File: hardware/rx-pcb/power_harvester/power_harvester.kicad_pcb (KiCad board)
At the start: 2 copper layers, 59 x 46.8 mm, 46 parts, among them J1 Conn_Coaxial_Small, J2 Conn_01x02_Pin, J3 Conn_Coaxial_Small, J4 Conn_Coaxial_Small

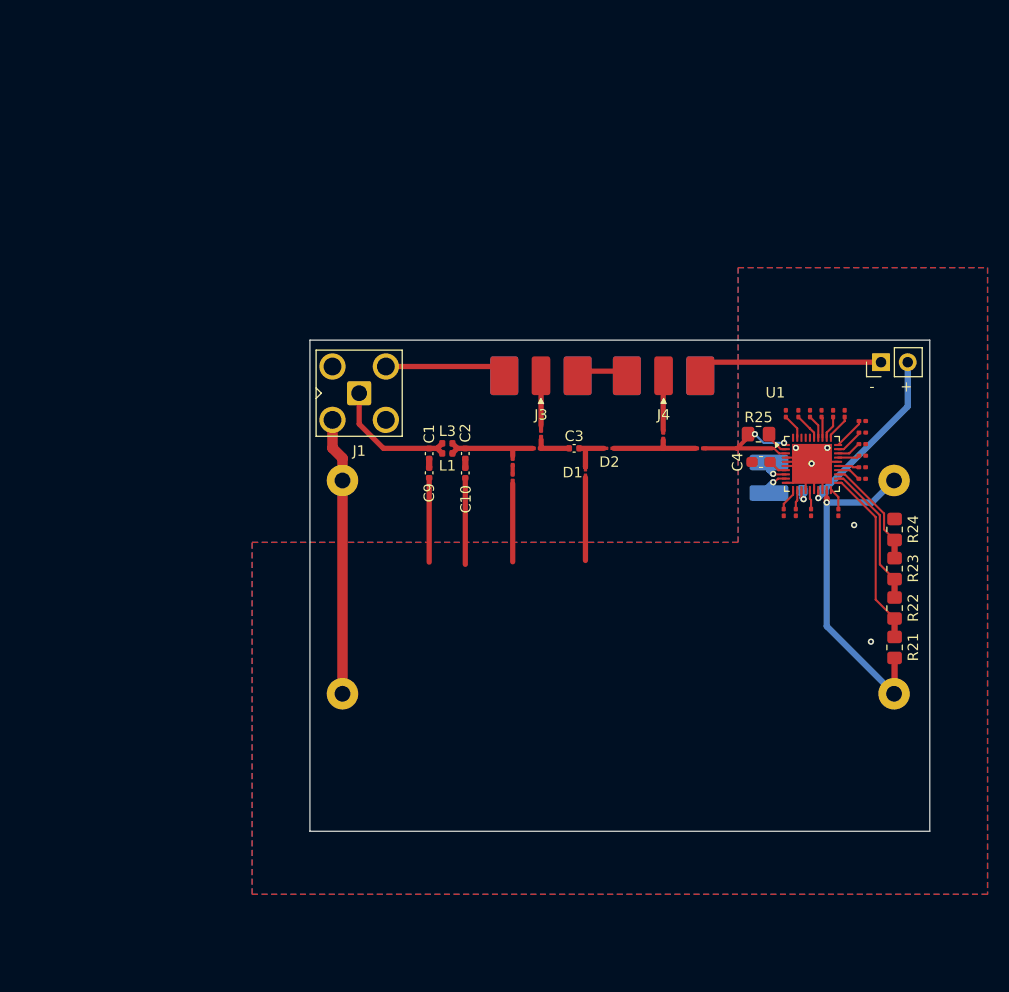
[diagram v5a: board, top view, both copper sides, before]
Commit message: updated PCB for weeks purchase
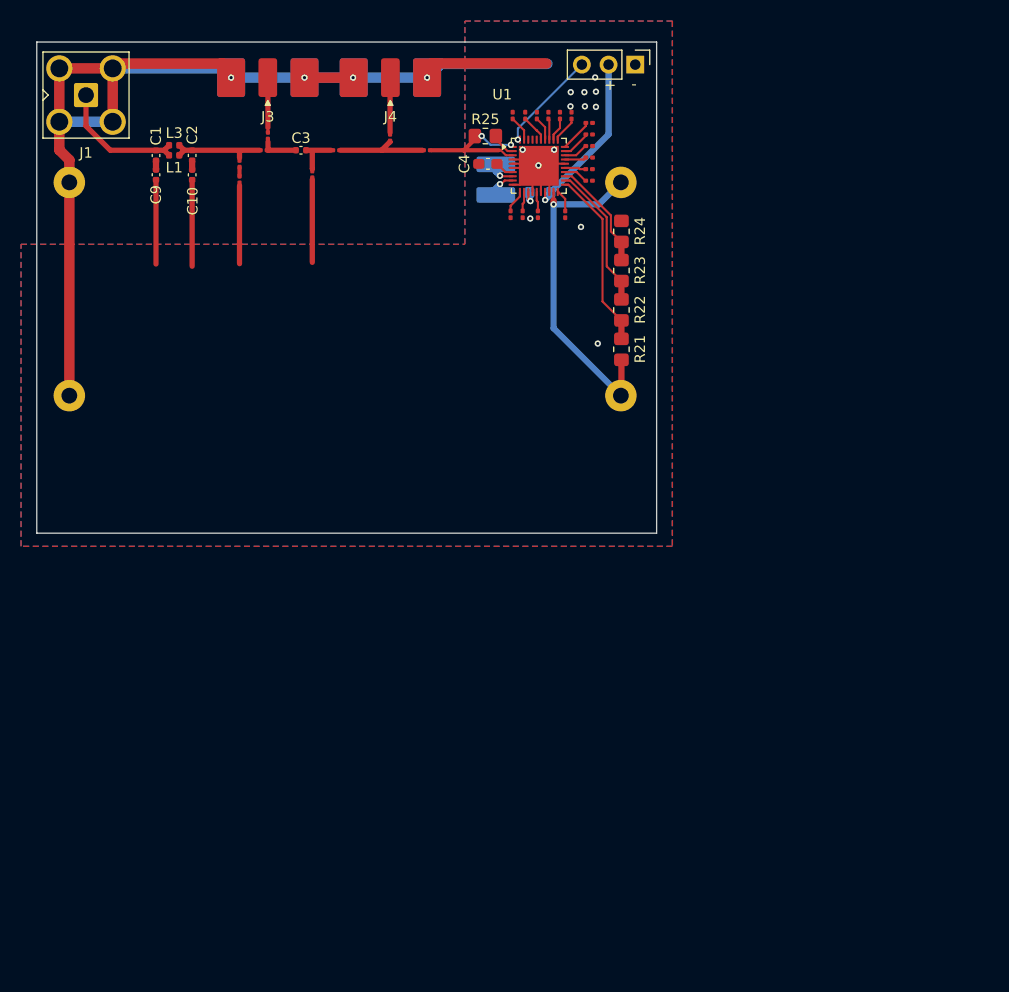
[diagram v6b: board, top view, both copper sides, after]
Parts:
- removed J2: Conn_01x02_Pin, Connector_PinHeader_2.54mm:PinHeader_1x02_P2.54mm_Vertical
- added J5: Conn_01x03_Pin, Connector_PinHeader_2.54mm:PinHeader_1x03_P2.54mm_Vertical, F.Cu at (127.5, 48.8)
- D1, D2: footprint power_harvester:JDH2S02SL -> power_harvester:R_0201_0603Metric_correctedclearance
- D3, D4: footprint Capacitor_SMD:C_0201_0603Metric -> power_harvester:R_0201_0603Metric_correctedclearance
- R1, R10, R11, R12, R13, R14, R15, R16, R2, R3, R4, R5, R6, R7, R8, R9: footprint Resistor_SMD:R_0201_0603Metric -> power_harvester:R_0201_0603Metric_correctedclearance
- R17, R18, R19, R20: footprint Resistor_SMD:R_0201_0603Metric_Pad0.64x0.40mm_HandSolder -> power_harvester:R_0201_0603Metric_correctedclearance
- moved C5 38.5 mm to (117.4, 60.1)
- moved C6 38.5 mm to (119.4, 60.1)
- moved R1 38.5 mm to (123.1, 56.5)
- moved R11 38.5 mm to (120.8, 63.0)
- moved C2 38.5 mm to (85.3, 57.4)
- moved R15 38.5 mm to (123.1, 54.3)
- moved R19 38.5 mm to (92.5, 55.5)
- moved R3 38.5 mm to (123.1, 57.6)
- moved R5 38.5 mm to (120.3, 53.6)
- moved R6 38.5 mm to (116.8, 63.0)
- moved R7 38.5 mm to (115.6, 63.0)
- moved R8 38.5 mm to (115.8, 53.6)
- moved R9 38.5 mm to (123.1, 55.4)
- moved C1 38.5 mm to (81.8, 57.4)
- moved C10 38.5 mm to (85.3, 59.3)
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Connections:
- U1 pad 40: unconnected-(U1-ST_STO-Pad40) -> /Pg
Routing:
- net GND: track 114.5 -> 173.3 mm, vias 5 -> 17
- net /Pg: track 0.00 -> 10.3 mm, vias 0 -> 1
- net /Po: track 17.4 -> 16.3 mm

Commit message: minor harvester updates
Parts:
- R12, R13, R4: value on -> off
- R14: value off -> on
- R21: value x -> 0
- R22: value x -> 19.5M
- R23: value x -> 100k
- R24: value x -> 5.6M
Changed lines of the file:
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@@
 		)
 		(property "Value" "off"
-			(at 0 1.05 180)
+			(at -1.705 0.025 180)
 			(layer "F.Fab")
 			(effects
@@
 			)
 		)
-		(property "Value" "x"
+		(property "Value" "100k"
 			(at 0 1.65 90)
 			(layer "F.Fab")
@@
 			)
 		)
-		(property "Value" "on"
-			(at 0 1.05 180)
+		(property "Value" "off"
+			(at -1.705 0.025 180)
 			(layer "F.Fab")
 			(effects
@@
 		)
 		(property "Value" "off"
-			(at 0 1.05 180)
+			(at -1.705 0.025 180)
 			(layer "F.Fab")
 			(effects
@@
 		)
 		(property "Value" "Conn_01x03_Pin"
-			(at 0 7.460001 90)
+			(at 4.55 0.465 90)
 			(layer "F.Fab")
+			(hide yes)
 			(effects
 				(font
@@
 			)
 		)
-		(property "Value" "off"
-			(at 0 1.05 180)
+		(property "Value" "on"
+			(at -1.705 0.025 180)
 			(layer "F.Fab")
 			(effects
@@
 			)
 		)
-		(property "Value" "on"
-			(at 0 1.05 270)
+		(property "Value" "off"
+			(at -1.75 0.025 270)
 			(layer "F.Fab")
 			(effects
@@
 			)
 		)
-		(property "Value" "x"
+		(property "Value" "5.6M"
 			(at 0 1.65 90)
 			(layer "F.Fab")
@@
 			)
 		)
-		(property "Value" "x"
+		(property "Value" "19.5M"
 			(at 0 1.65 90)
 			(layer "F.Fab")
@@
 			)
 		)
-		(property "Value" "on"
-			(at 0 1.05 270)
+		(property "Value" "off"
+			(at -1.75 0.025 270)
 			(layer "F.Fab")
 			(effects
@@
 		)
 		(property "Value" "on"
-			(at 0 1.05 90)
+			(at -1.725 -0.1 90)
 			(layer "F.Fab")
 			(effects
@@
 		)
 		(property "Value" "off"
-			(at 0 1.05 90)
+			(at -1.725 -0.1 90)
 			(layer "F.Fab")
 			(effects
@@
 		)
 		(property "Value" "off"
-			(at 0 1.05 270)
+			(at -1.75 0.025 270)
 			(layer "F.Fab")
 			(effects
@@
 			)
 		)
-		(property "Value" "x"
+		(property "Value" "0"
 			(at 0 1.65 90)
 			(layer "F.Fab")
@@
 		)
 		(property "Value" "on"
-			(at 0 1.05 180)
+			(at -1.705 0.025 180)
 			(layer "F.Fab")
 			(effects
@@
 		)
 		(property "Value" "off"
-			(at 0 1.05 270)
+			(at -1.75 0.025 270)
 			(layer "F.Fab")
 			(effects
@@
 		)
 		(property "Value" "on"
-			(at 0 1.05 270)
+			(at -1.75 0.025 270)
 			(layer "F.Fab")
 			(effects
@@
 		)
 		(property "Value" "on"
-			(at 0 1.05 90)
+			(at -1.725 -0.1 90)
 			(layer "F.Fab")
 			(effects
@@
 		)
 		(property "Value" "off"
-			(at 0 1.05 90)
+			(at -1.725 -0.1 90)
 			(layer "F.Fab")
 			(effects
@@
 		)
 		(property "Value" "on"
-			(at 0 1.05 180)
+			(at -1.705 0.025 180)
 			(layer "F.Fab")
 			(effects
@@
 		)
 		(property "Value" "on"
-			(at 0 1.05 270)
+			(at -1.75 0.025 270)
 			(layer "F.Fab")
 			(effects

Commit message: updated power harvester hardware program
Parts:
- R25: value x -> 1k
- R6, R7: value on -> off
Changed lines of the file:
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@@
 			)
 		)
-		(property "Value" "on"
+		(property "Value" "off"
 			(at -1.725 -0.1 90)
 			(layer "F.Fab")
@@
 			)
 		)
-		(property "Value" "x"
+		(property "Value" "1k"
 			(at 0 1.65 0)
 			(layer "F.Fab")
@@
 			)
 		)
-		(property "Value" "on"
+		(property "Value" "off"
 			(at -1.725 -0.1 90)
 			(layer "F.Fab")
